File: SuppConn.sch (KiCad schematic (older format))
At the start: 13 parts, among them J5 SuppPowerConnector, U6 REF34-Q1, U7 OPAx192-Q1, U8 OPA388-Q1, U9 OPA388-Q1

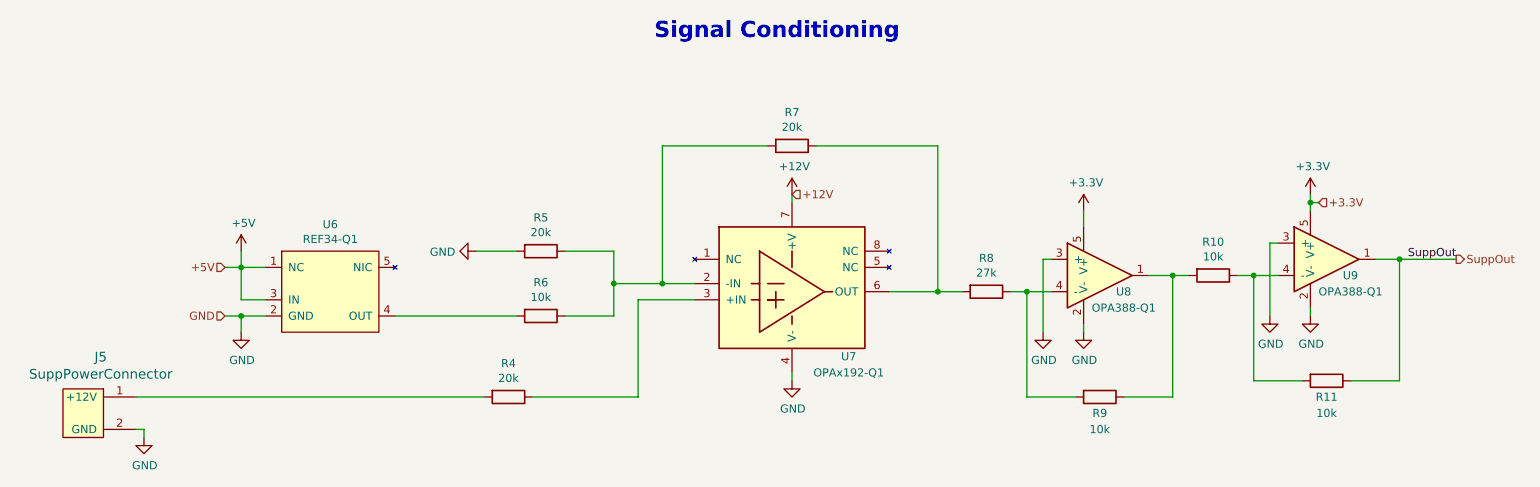
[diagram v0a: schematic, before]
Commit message: Makes edits from critical design review
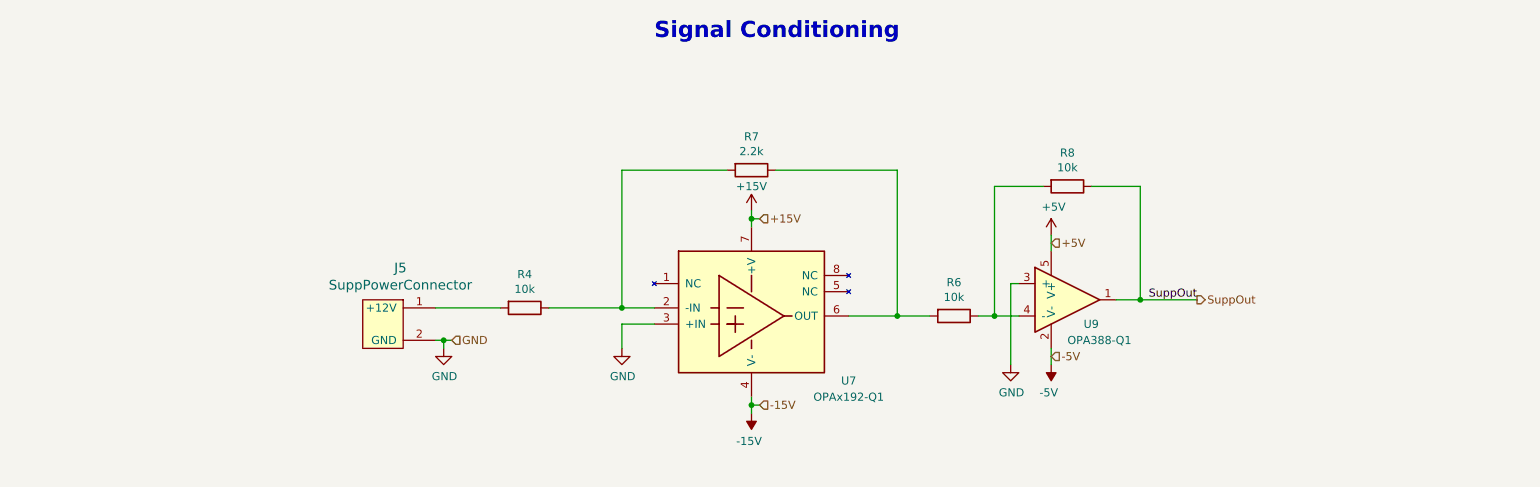
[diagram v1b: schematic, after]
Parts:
- removed R10, R11, R9: 10k, Resistor_SMD:R_0805_2012Metric, symbol Device:R
- removed R5: 20k, Resistor_SMD:R_0805_2012Metric, symbol Device:R
- removed U6: REF34-Q1, Package_TO_SOT_SMD:SOT-23-5, symbol utsvt-chips:REF34-Q1
- removed U8: OPA388-Q1, Package_TO_SOT_SMD:SOT-23-5, symbol utsvt-chips:OPA388-Q1
- R4: value 20k -> 10k
- R7: value 20k -> 2.2k
- R8: value 27k -> 10k
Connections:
- net +3V3 is gone; now on net +5V: U9.5 (V+)
- net GND: now also U7.3 (+IN); no longer U7.4 (V-), U9.2 (V-)
- net SuppOut: now also R8.1
- net at R7.2, U7.2 (-IN): now also R4.1; no longer R6.1
- net at R6.2: now also R7.1, U7.6 (OUT)
- net at U9.4 (-): now also R6.1, R8.2
- net +12V renamed +15V
- new net -15V: U7.4 (V-)
- new net -5V: U9.2 (V-)
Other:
- moved on the sheet: J5, R4, R7, U7
